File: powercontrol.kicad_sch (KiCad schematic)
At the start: 14 parts, among them J1 Conn_01x01, J11 Conn_01x01, J2 Conn_01x01, K1 Relay_SPST-NO, P1 Conn_01x01, P11 Conn_01x01, P2 Conn_01x01, Q2 MMBT3904

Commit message: Looking quite accurate. Time to fix connector foots.
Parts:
- renumbered K1 to SW1
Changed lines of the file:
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@@
 		(dnp no)
 		(fields_autoplaced yes)
-		(property "Reference" "K1"
+		(property "Reference" "SW1"
 			(at 151.13 44.45 90)
 			(effects
@@
 			(project ""
 				(path "/0188b917-fce8-4efb-9412-06c57849f476/0ab46fdb-7cb6-401b-9809-d46422bb951a"
-					(reference "K1")
+					(reference "SW1")
 					(unit 1)
 				)

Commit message: Added vias. Proper connector holes for socket and plug. Now final cleanups mostly.
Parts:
- J1, J2: footprint Connector_PinHeader_1.00mm:PinHeader_1x01_P1.00mm_Vertical -> designfootprints:NEMA_5P_pin
- P1, P2: footprint Connector_PinHeader_1.00mm:PinHeader_1x01_P1.00mm_Vertical -> designfootprints:NEMA_5R_slot
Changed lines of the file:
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@@
 			)
 		)
-		(property "Footprint" "Connector_PinHeader_1.00mm:PinHeader_1x01_P1.00mm_Vertical"
+		(property "Footprint" "designfootprints:NEMA_5R_slot"
 			(at 157.48 138.43 0)
 			(effects
@@
 			)
 		)
-		(property "Footprint" "Connector_PinHeader_1.00mm:PinHeader_1x01_P1.00mm_Vertical"
+		(property "Footprint" "designfootprints:NEMA_5P_pin"
 			(at 99.06 138.43 0)
 			(effects
@@
 			)
 		)
-		(property "Footprint" "Connector_PinHeader_1.00mm:PinHeader_1x01_P1.00mm_Vertical"
+		(property "Footprint" "designfootprints:NEMA_5P_pin"
 			(at 99.06 152.4 0)
 			(effects
@@
 			)
 		)
-		(property "Footprint" "Connector_PinHeader_1.00mm:PinHeader_1x01_P1.00mm_Vertical"
+		(property "Footprint" "designfootprints:NEMA_5R_slot"
 			(at 157.48 152.4 0)
 			(effects

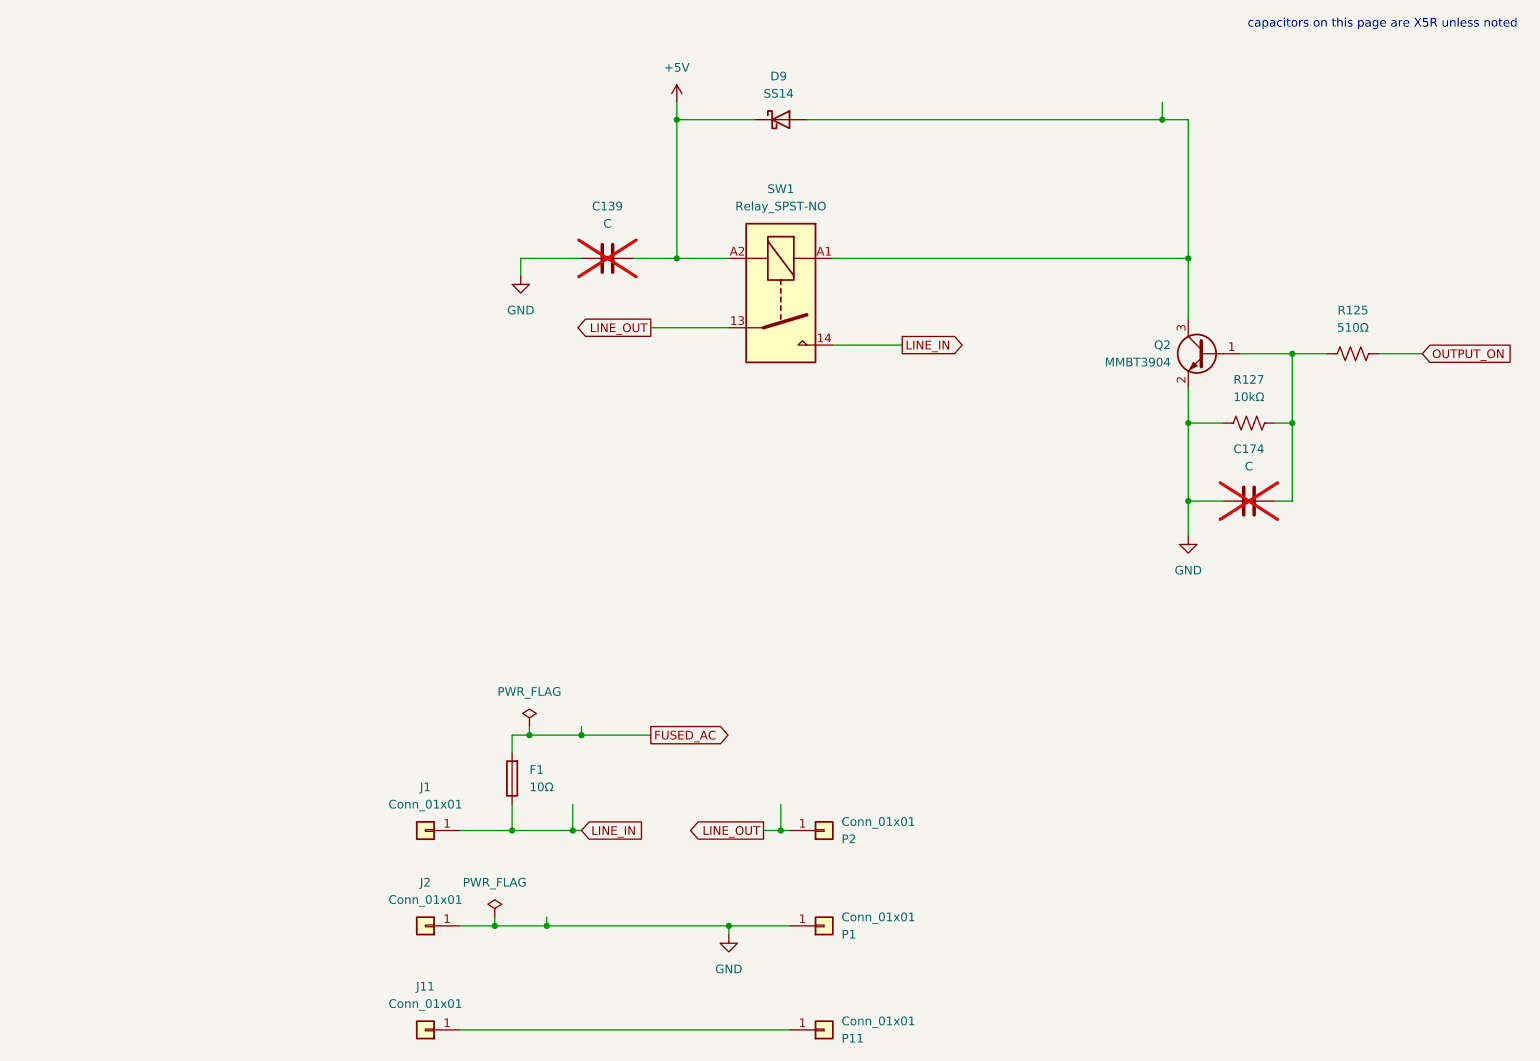
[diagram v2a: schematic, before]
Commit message: Cleaned schematic. Still have silk and fab to do. Also have not fixed F1. Have decided I may not fix F1.
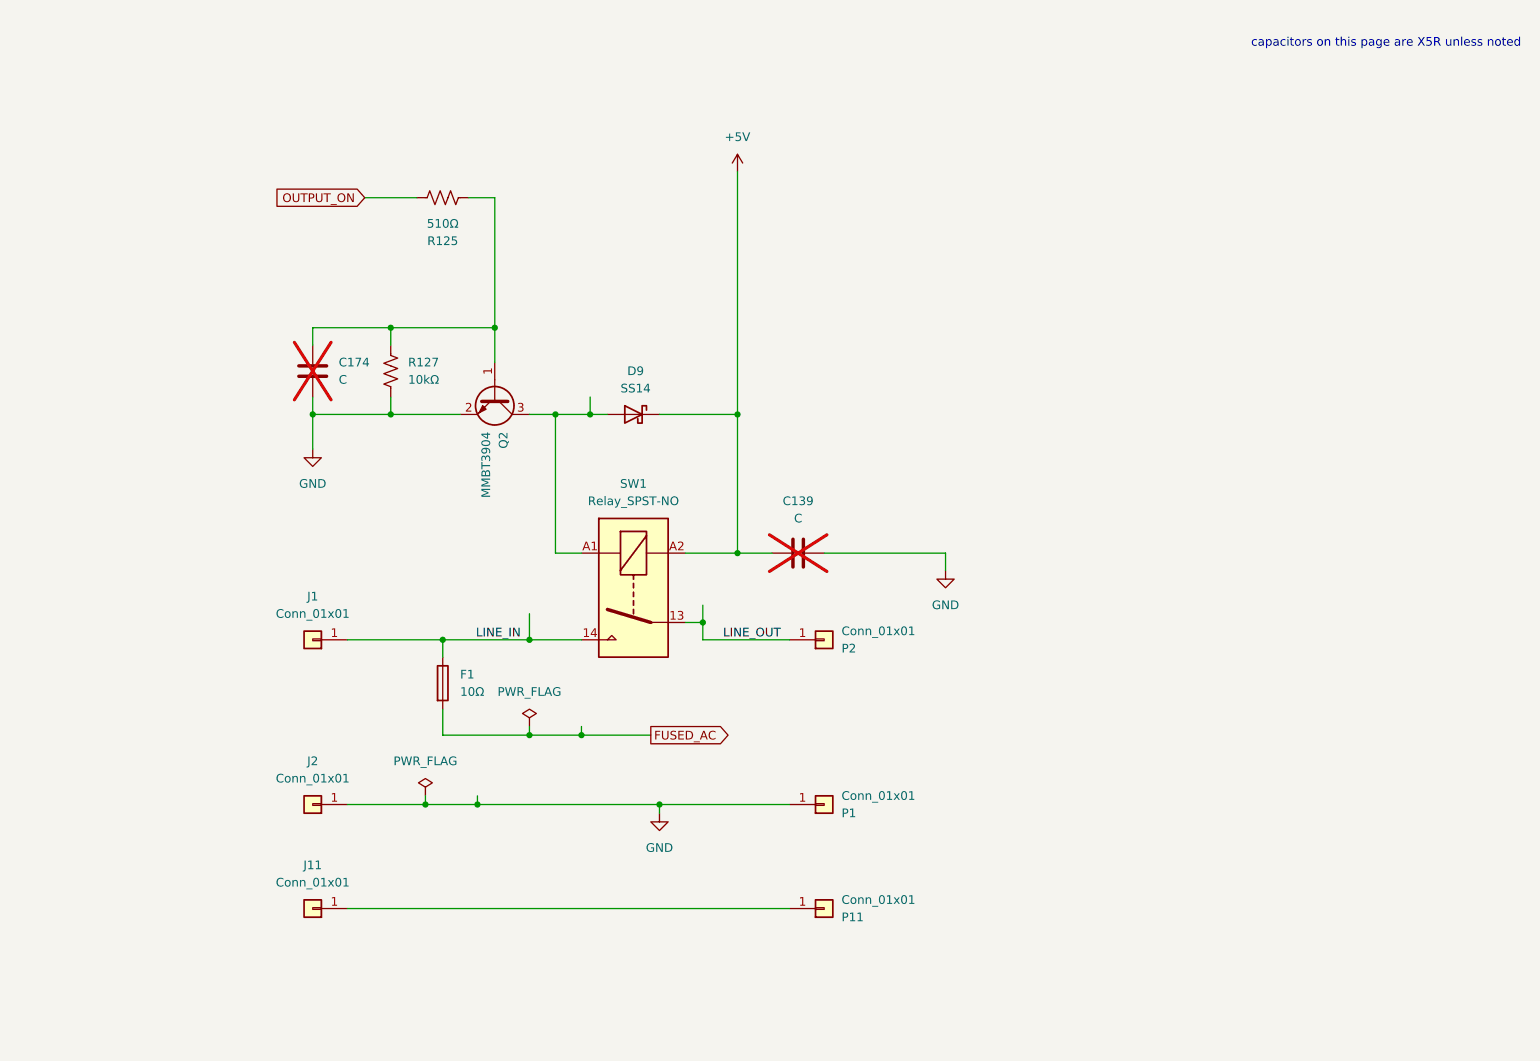
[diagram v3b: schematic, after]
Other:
- title: (none) -> T smart switched power outlet
- moved on the sheet: C139, C174, D9, F1, J1, J11, J2, P1, P11, P2, Q2, R125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

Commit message: Added description of microcontroller subboard to schematic.
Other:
- note added: "F1 is RFS series"
- note added: "OUTLET GROUND"
- note added: "OUTLET HOT"
- note added: "OUTLET NEUTRAL"
- note added: "SUPPLY HOT"
- note added: "SUPPLY NEUTRAL"
- note added: "SUPPLY PROTECTIVE GROUND"
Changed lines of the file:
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@@
 		(title "T smart switched power outlet")
+	)
+	(text "SUPPLY NEUTRAL"
+		(exclude_from_sim no)
+		(at 70.358 134.62 0)
+		(effects
+			(font
+				(size 1.27 1.27)
+			)
+			(justify right)
+		)
+	)
+	(text "F1 is RFS series"
+		(exclude_from_sim no)
+		(at 84.582 120.65 0)
+		(effects
+			(font
+				(size 1.27 1.27)
+			)
+		)
+	)
+	(text "OUTLET GROUND"
+		(exclude_from_sim no)
+		(at 176.784 149.86 0)
+		(effects
+			(font
+				(size 1.27 1.27)
+			)
+			(justify left)
+		)
+	)
+	(text "OUTLET NEUTRAL"
+		(exclude_from_sim no)
+		(at 176.784 134.874 0)
+		(effects
+			(font
+				(size 1.27 1.27)
+			)
+			(justify left)
+		)
+	)
+	(text "SUPPLY HOT"
+		(exclude_from_sim no)
+		(at 69.088 111.252 0)
+		(effects
+			(font
+				(size 1.27 1.27)
+			)
+			(justify right)
+		)
+	)
+	(text "SUPPLY PROTECTIVE GROUND"
+		(exclude_from_sim no)
+		(at 70.612 149.098 0)
+		(effects
+			(font
+				(size 1.27 1.27)
+			)
+			(justify right)
+		)
+	)
+	(text "OUTLET HOT"
+		(exclude_from_sim no)
+		(at 177.292 110.49 0)
+		(effects
+			(font
+				(size 1.27 1.27)
+			)
+			(justify left)
+		)
 	)
 	(text "capacitors on this page are X5R unless noted"

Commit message: Updating project to describe itself better.
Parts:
- R125: value 510Ω -> 510
- R127: value 10kΩ -> 10k
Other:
- note added: "capacitors on this page are 10V X5R unless noted"
- note removed: "capacitors on this page are X5R unless noted"
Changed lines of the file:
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@@
 		)
 	)
-	(text "capacitors on this page are X5R unless noted"
+	(text "capacitors on this page are 10V X5R unless noted"
 		(exclude_from_sim no)
 		(at 259.588 23.114 0)
@@
 		(fields_autoplaced yes)
 		(property "Reference" "R125"
-			(at 101.6 52.07 90)
-			(effects
-				(font
-					(size 1.27 1.27)
-				)
-			)
-		)
-		(property "Value" "510Ω"
-			(at 101.6 49.53 90)
+			(at 101.6 39.37 90)
+			(effects
+				(font
+					(size 1.27 1.27)
+				)
+			)
+		)
+		(property "Value" "510"
+			(at 101.6 41.91 90)
 			(effects
 				(font
@@
 			)
 		)
-		(property "Value" "10kΩ"
+		(property "Value" "10k"
 			(at 96.52 72.3899 0)
 			(effects
